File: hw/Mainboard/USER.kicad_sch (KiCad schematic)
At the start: 1 part, among them J4 USER

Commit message: hw: wip add MCU, 2 layer board
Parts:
- J4: footprint PET:EDGE_CON_24P_USER -> Retrocomputing:CBM_PET_USER_EDGE_CON_24P; symbol Mainboard-rescue:Conn_02x12_Card_Edge-PET -> Retrocomputing:CBM_PET_USER_Conn_02x12_Card_Edge
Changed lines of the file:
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@@
     (effects (font (size 1.27 1.27)) (justify right))
   )
-  (symbol (lib_id "Mainboard-rescue:Conn_02x12_Card_Edge-PET") (at 133.35 69.85 0) (unit 1)
+  (symbol (lib_id "Retrocomputing:CBM_PET_USER_Conn_02x12_Card_Edge") (at 133.35 69.85 0) (unit 1)
     (in_bom yes) (on_board yes)
     (property "Reference" "J4" (id 0) (at 134.62 51.6382 0))
     (property "Value" "USER" (id 1) (at 134.62 53.9496 0))
-    (property "Footprint" "PET:EDGE_CON_24P_USER" (id 2) (at 133.35 69.85 0)
+    (property "Footprint" "Retrocomputing:CBM_PET_USER_EDGE_CON_24P" (id 2) (at 133.35 69.85 0)
       (effects (font (size 1.27 1.27)) hide)
     )

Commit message: hw: routable (wip)
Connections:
- net GND renamed PD_GND

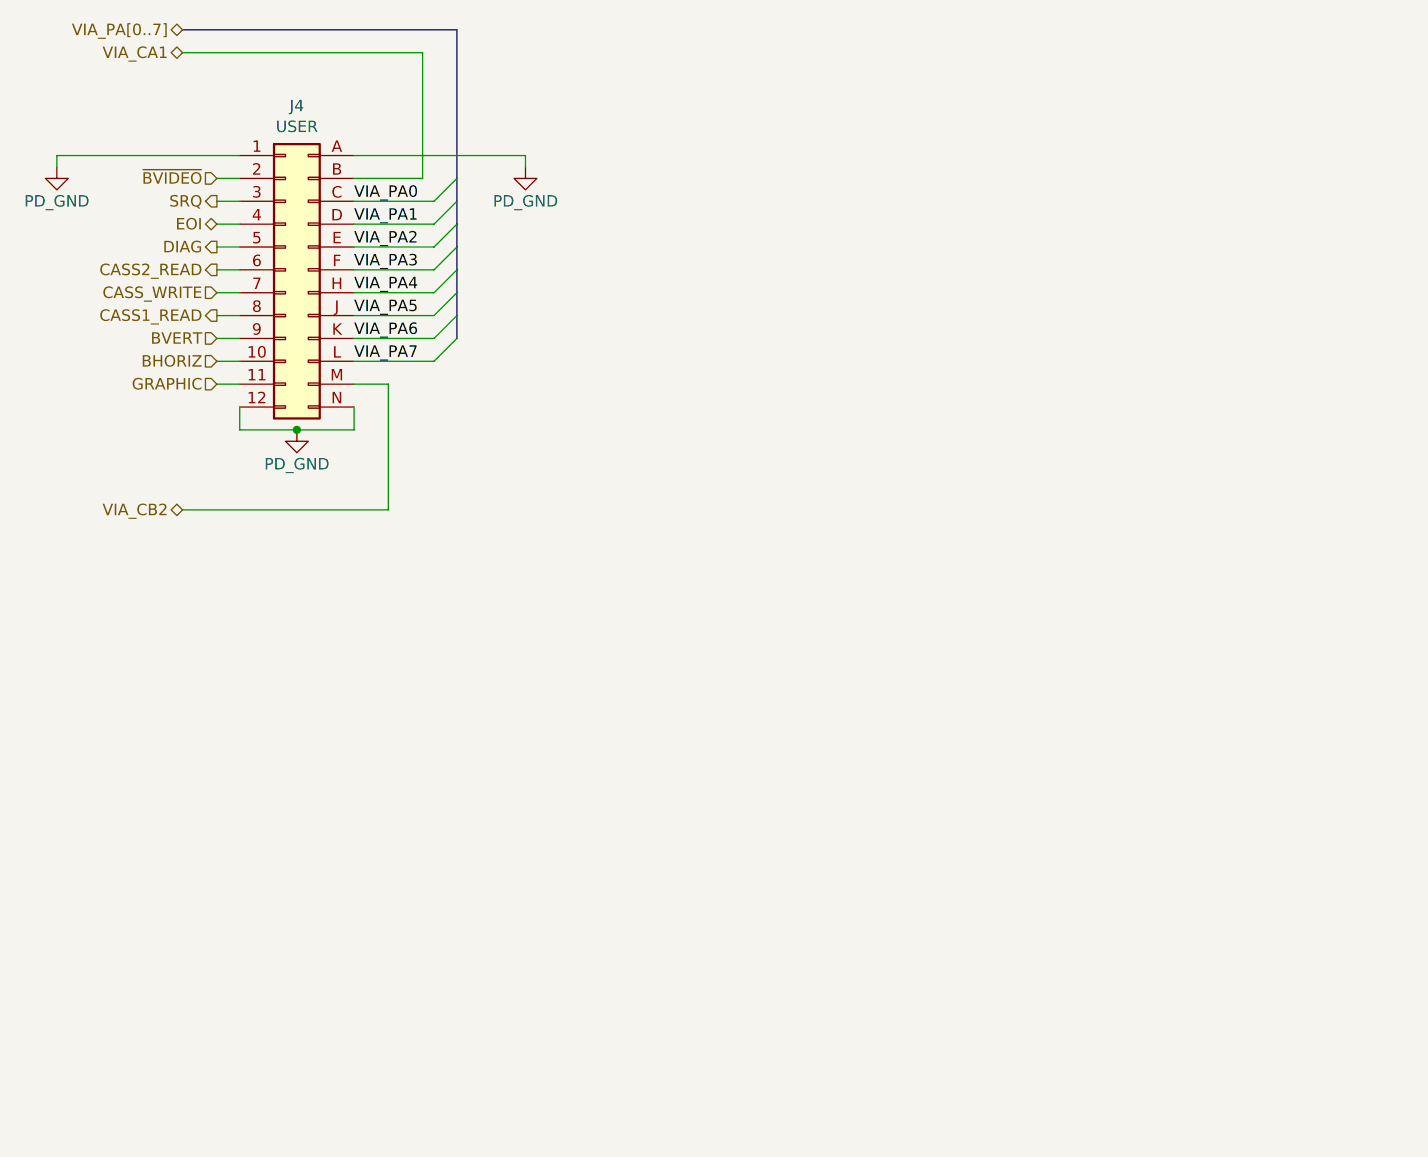
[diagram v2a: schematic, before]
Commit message: hw: larger schematic pages, routed w/netties
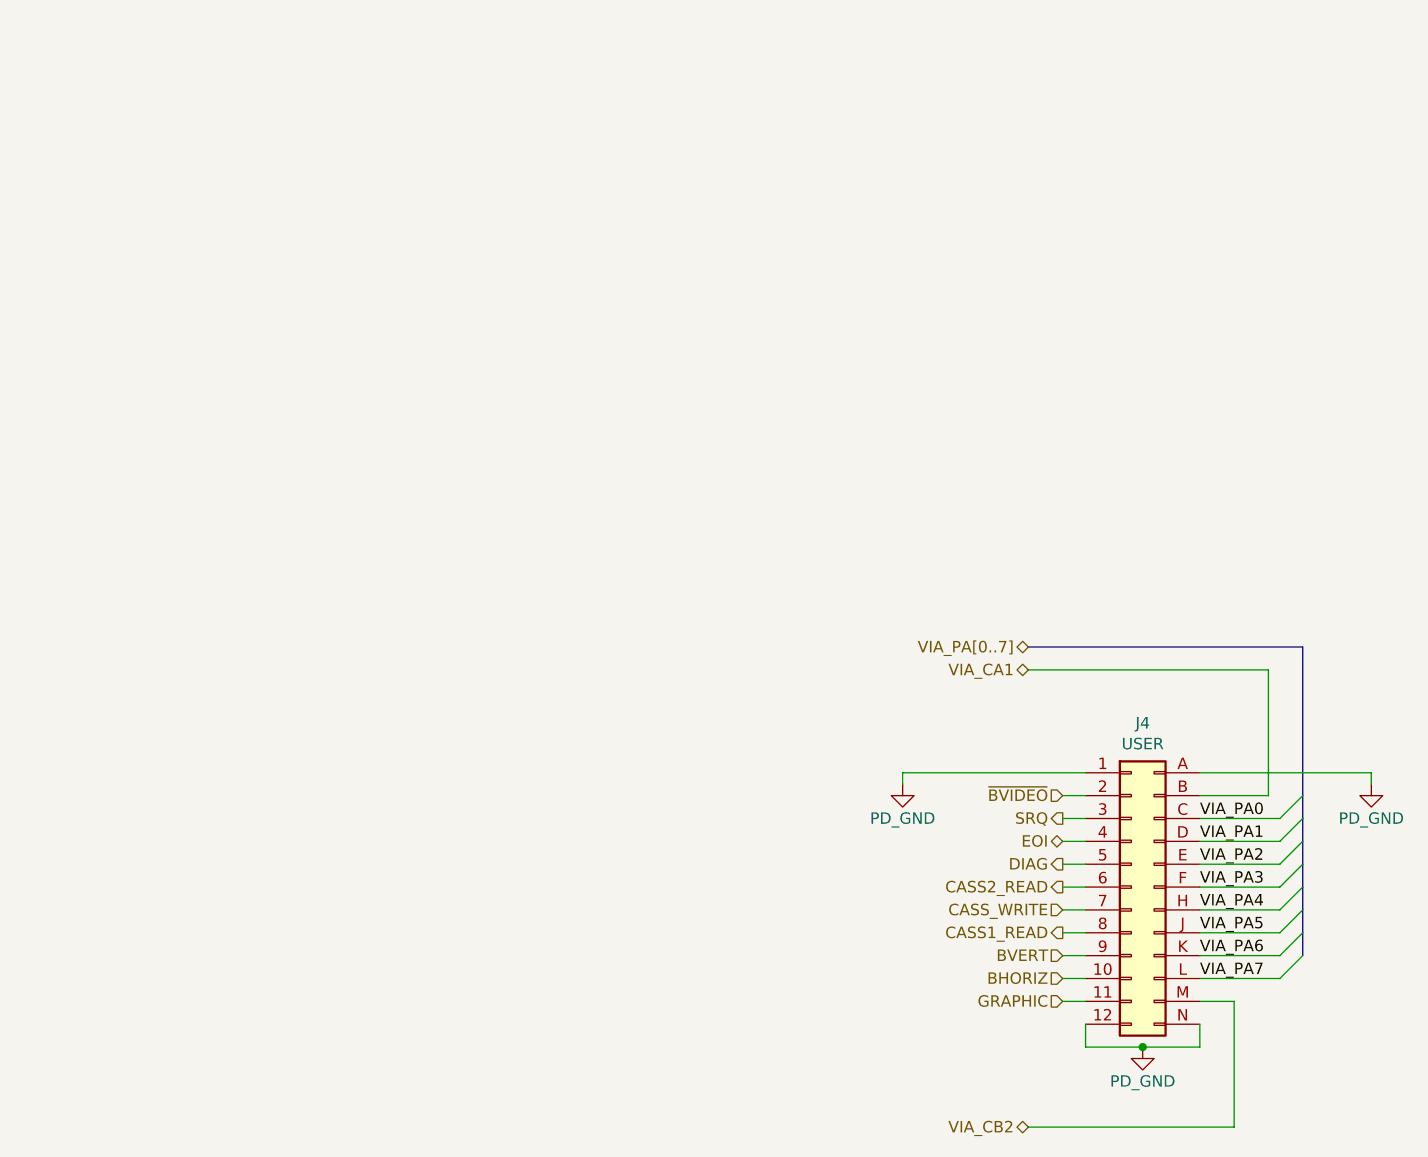
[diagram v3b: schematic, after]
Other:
- moved on the sheet: J4

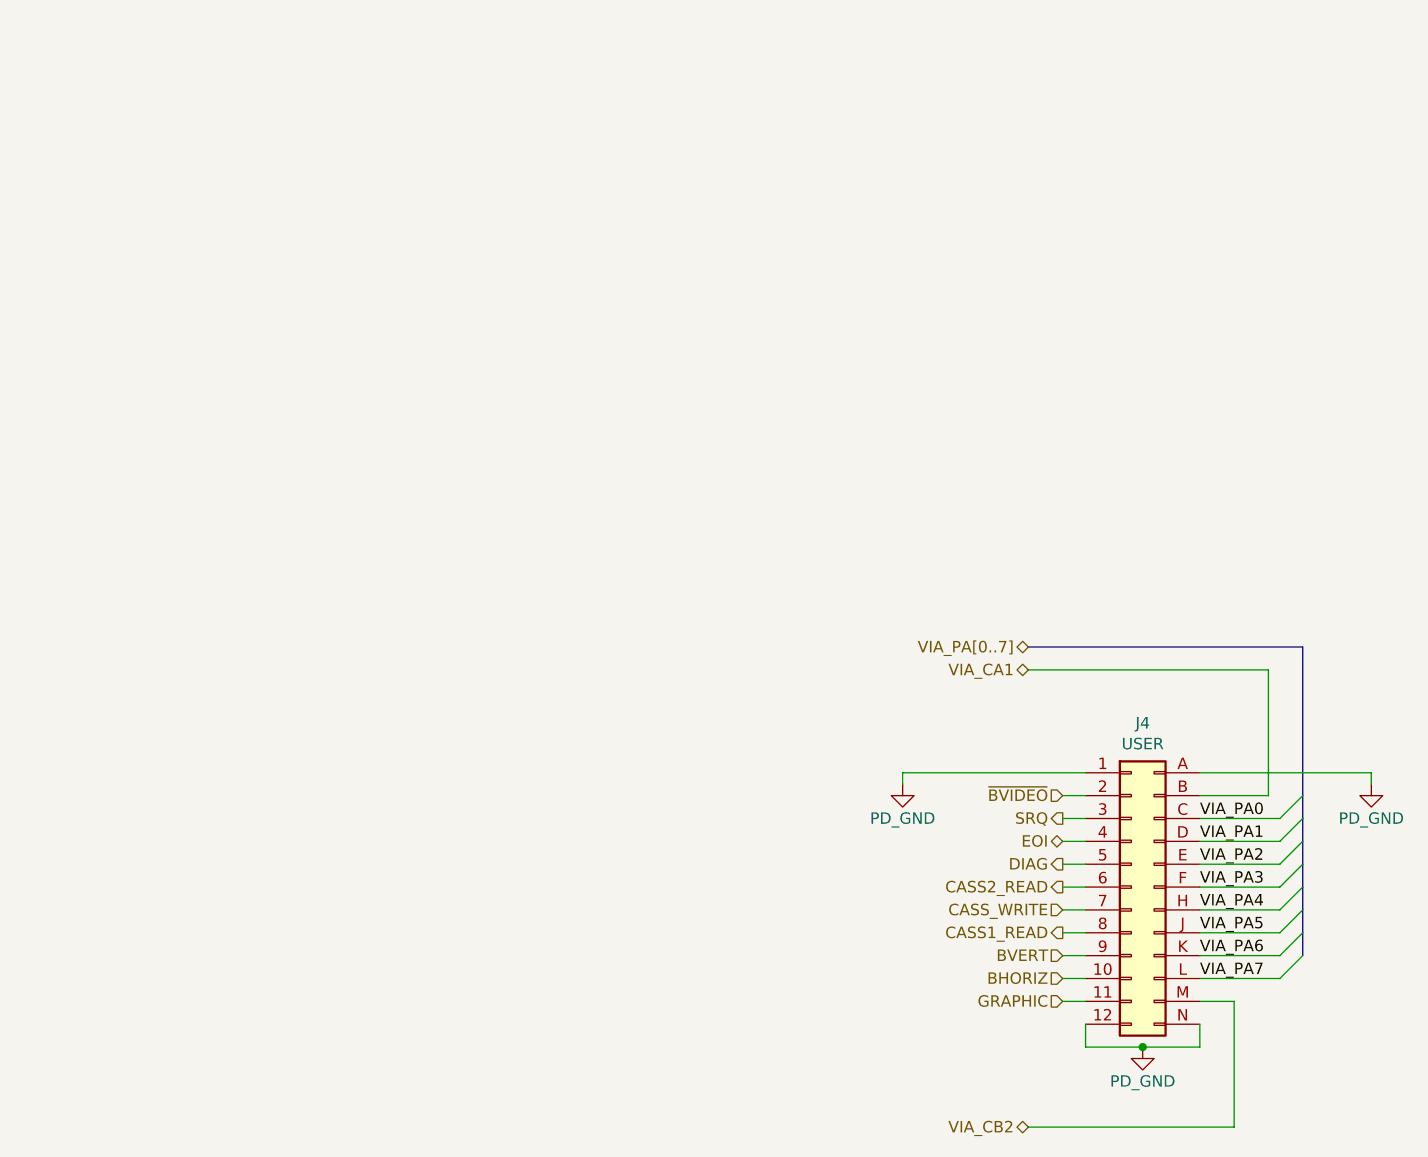
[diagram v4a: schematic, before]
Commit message: hw: tidy power and resize pages
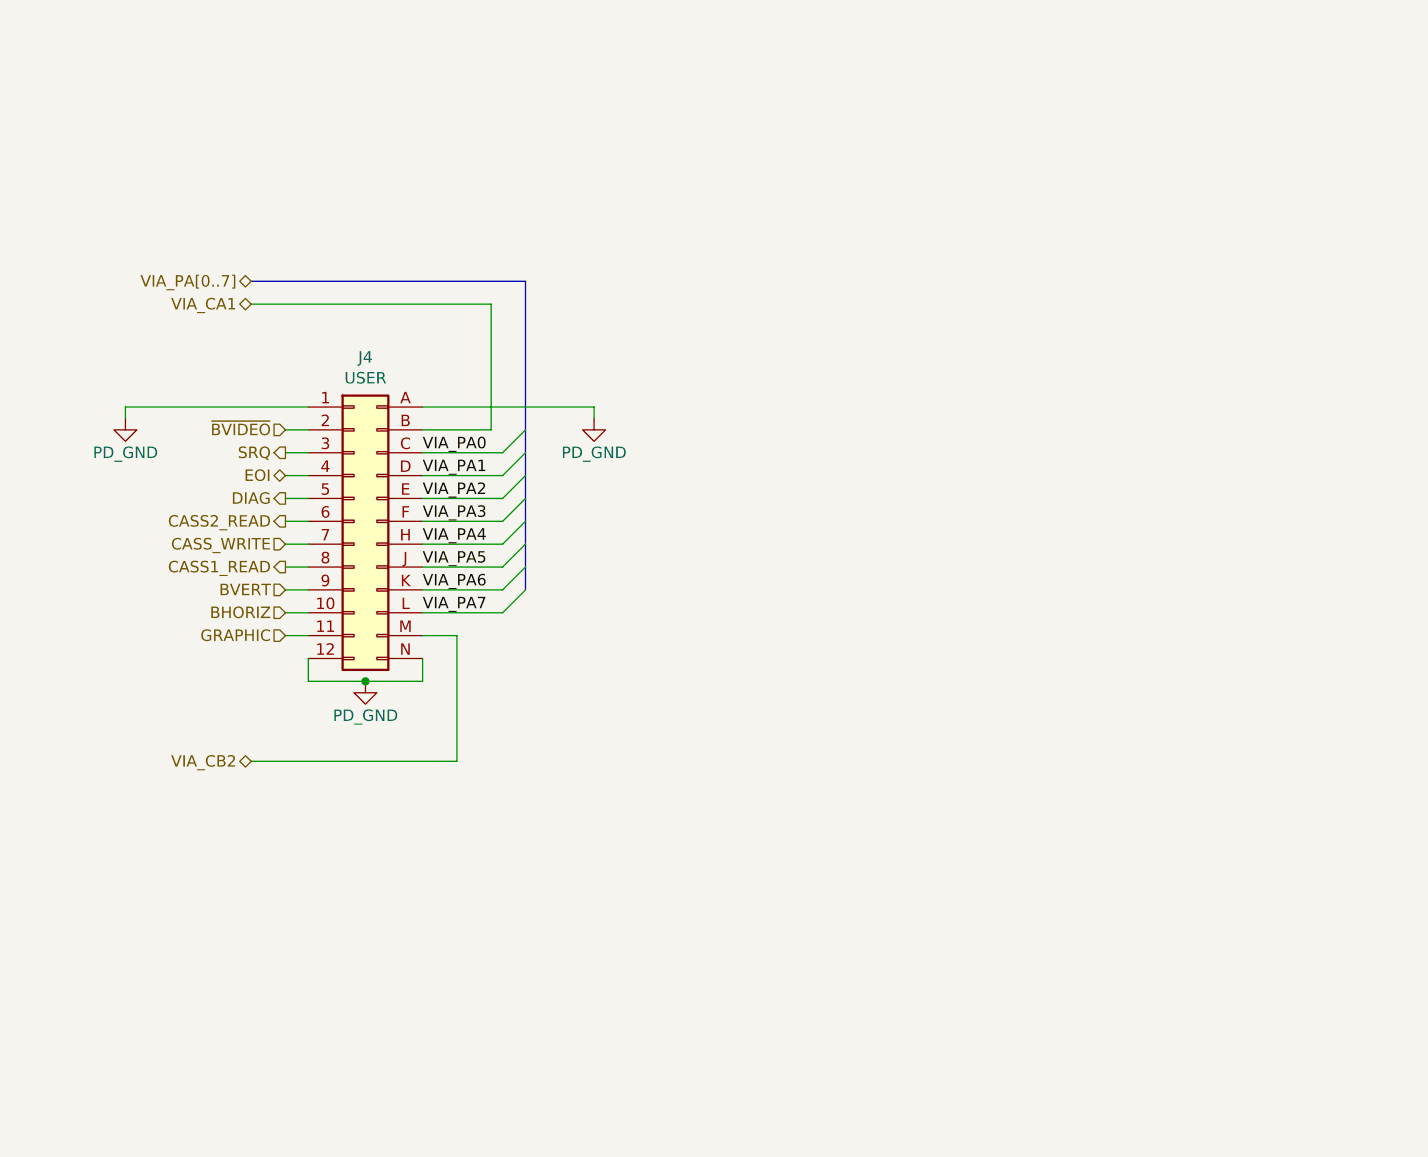
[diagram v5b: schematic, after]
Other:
- title: (none) -> CBM PET Mainboard Replacement
- moved on the sheet: J4

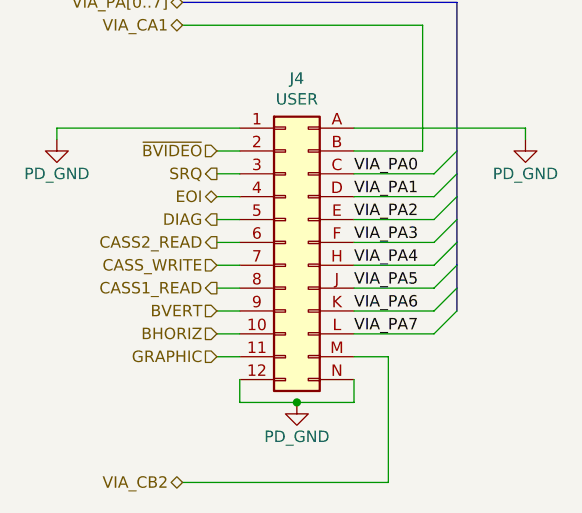
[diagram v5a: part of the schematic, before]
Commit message: hw: tidy audio, cass, IEEE, keyboard, magic, user
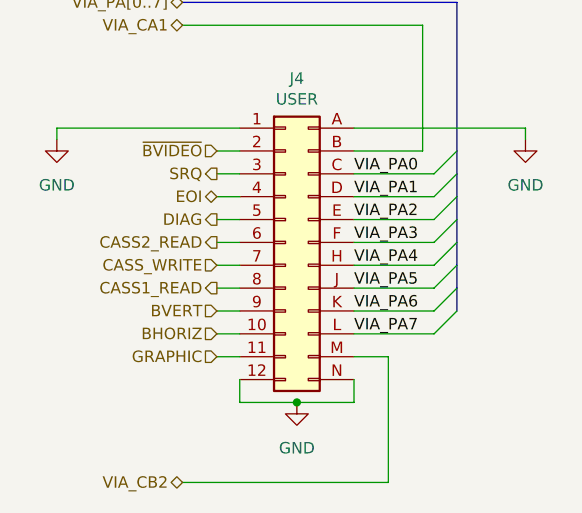
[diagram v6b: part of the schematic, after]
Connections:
- net PD_GND renamed GND
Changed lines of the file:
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@@
-    (stroke (width 0) (type default) (color 0 0 0 0))
-  )
-  (wire (pts (xy 142.24 115.57) (xy 148.59 115.57))
     (stroke (width 0) (type default) (color 0 0 0 0))
   )
@@
   )
   (wire (pts (xy 167.64 85.09) (xy 167.64 86.36))
+    (stroke (width 0) (type default) (color 0 0 0 0))
+  )
+  (wire (pts (xy 142.24 115.57) (xy 148.59 115.57))
     (stroke (width 0) (type default) (color 0 0 0 0))
   )
@@
     (pin "N")
   )
-  (symbol (lib_id "PET:PD_GND") (at 115.57 86.36 0) (unit 1)
-    (in_bom yes) (on_board yes)
-    (property "Reference" "#PWR0187" (id 0) (at 115.57 92.71 0)
+  (symbol (lib_id "power:GND") (at 115.57 86.36 0) (unit 1)
+    (in_bom yes) (on_board yes) (fields_autoplaced)
+    (property "Reference" "#PWR?" (id 0) (at 115.57 92.71 0)
       (effects (font (size 1.27 1.27)) hide)
     )
-    (property "Value" "PD_GND" (id 1) (at 115.57 90.17 0))
+    (property "Value" "GND" (id 1) (at 115.57 91.44 0))
     (property "Footprint" "" (id 2) (at 115.57 86.36 0)
       (effects (font (size 1.27 1.27)) hide)
@@
     (pin "1")
   )
-  (symbol (lib_id "PET:PD_GND") (at 142.24 115.57 0) (unit 1)
-    (in_bom yes) (on_board yes)
-    (property "Reference" "#PWR0186" (id 0) (at 142.24 121.92 0)
+  (symbol (lib_id "power:GND") (at 167.64 86.36 0) (unit 1)
+    (in_bom yes) (on_board yes) (fields_autoplaced)
+    (property "Reference" "#PWR?" (id 0) (at 167.64 92.71 0)
       (effects (font (size 1.27 1.27)) hide)
     )
-    (property "Value" "PD_GND" (id 1) (at 142.24 119.38 0))
+    (property "Value" "GND" (id 1) (at 167.64 91.44 0))
+    (property "Footprint" "" (id 2) (at 167.64 86.36 0)
+      (effects (font (size 1.27 1.27)) hide)
+    )
+    (property "Datasheet" "" (id 3) (at 167.64 86.36 0)
+      (effects (font (size 1.27 1.27)) hide)
+    )
+    (pin "1")
+  )
+  (symbol (lib_id "power:GND") (at 142.24 115.57 0) (unit 1)
+    (in_bom yes) (on_board yes) (fields_autoplaced)
+    (property "Reference" "#PWR?" (id 0) (at 142.24 121.92 0)
+      (effects (font (size 1.27 1.27)) hide)
+    )
+    (property "Value" "GND" (id 1) (at 142.24 120.65 0))
     (property "Footprint" "" (id 2) (at 142.24 115.57 0)
       (effects (font (size 1.27 1.27)) hide)
@@
       (effects (font (size 1.27 1.27)) hide)
     )
-    (pin "1")
-  )
-  (symbol (lib_id "PET:PD_GND") (at 167.64 86.36 0) (unit 1)
-    (in_bom yes) (on_board yes)
-    (property "Reference" "#PWR0185" (id 0) (at 167.64 92.71 0)
-      (effects (font (size 1.27 1.27)) hide)
-    )
-    (property "Value" "PD_GND" (id 1) (at 167.64 90.17 0))
-    (property "Footprint" "" (id 2) (at 167.64 86.36 0)
-      (effects (font (size 1.27 1.27)) hide)
-    )
-    (property "Datasheet" "" (id 3) (at 167.64 86.36 0)
-      (effects (font (size 1.27 1.27)) hide)
-    )

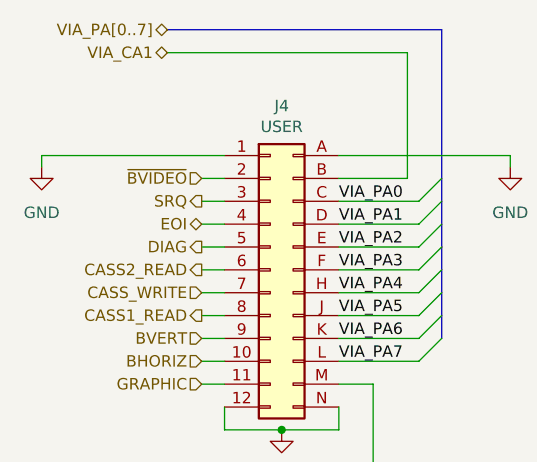
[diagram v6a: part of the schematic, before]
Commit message: hw: remove bar from video signal name
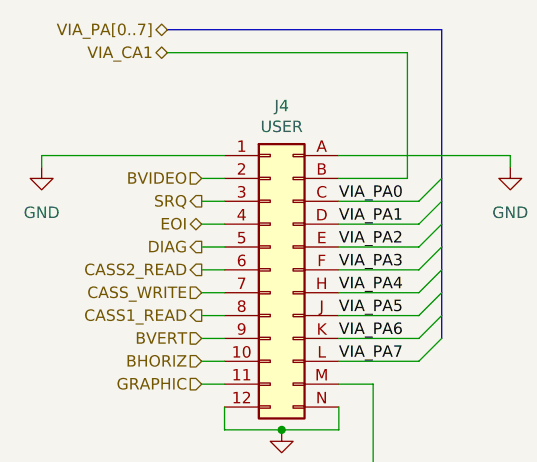
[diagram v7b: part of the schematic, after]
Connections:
- net ~{BVIDEO} renamed BVIDEO
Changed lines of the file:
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@@
     (effects (font (size 1.27 1.27)) (justify right))
   )
-  (hierarchical_label "~{BVIDEO}" (shape input) (at 133.35 87.63 180)
+  (hierarchical_label "BVIDEO" (shape input) (at 133.35 87.63 180)
     (effects (font (size 1.27 1.27)) (justify right))
   )
